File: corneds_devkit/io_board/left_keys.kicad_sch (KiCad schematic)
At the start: 42 parts, among them SW1 SW_Push, SW10 SW_Push, SW11 SW_Push, SW12 SW_Push, SW13 SW_Push, SW15 SW_Push, SW17 SW_Push, SW19 SW_Push, SW2 SW_Push, SW20 SW_Push, SW21 SW_Push, SW22 SW_Push, SW23 SW_Push, SW24 SW_Push, SW3 SW_Push, SW4 SW_Push, SW5 SW_Push, SW6 SW_Push, SW7 SW_Push, SW8 SW_Push, SW9 SW_Push

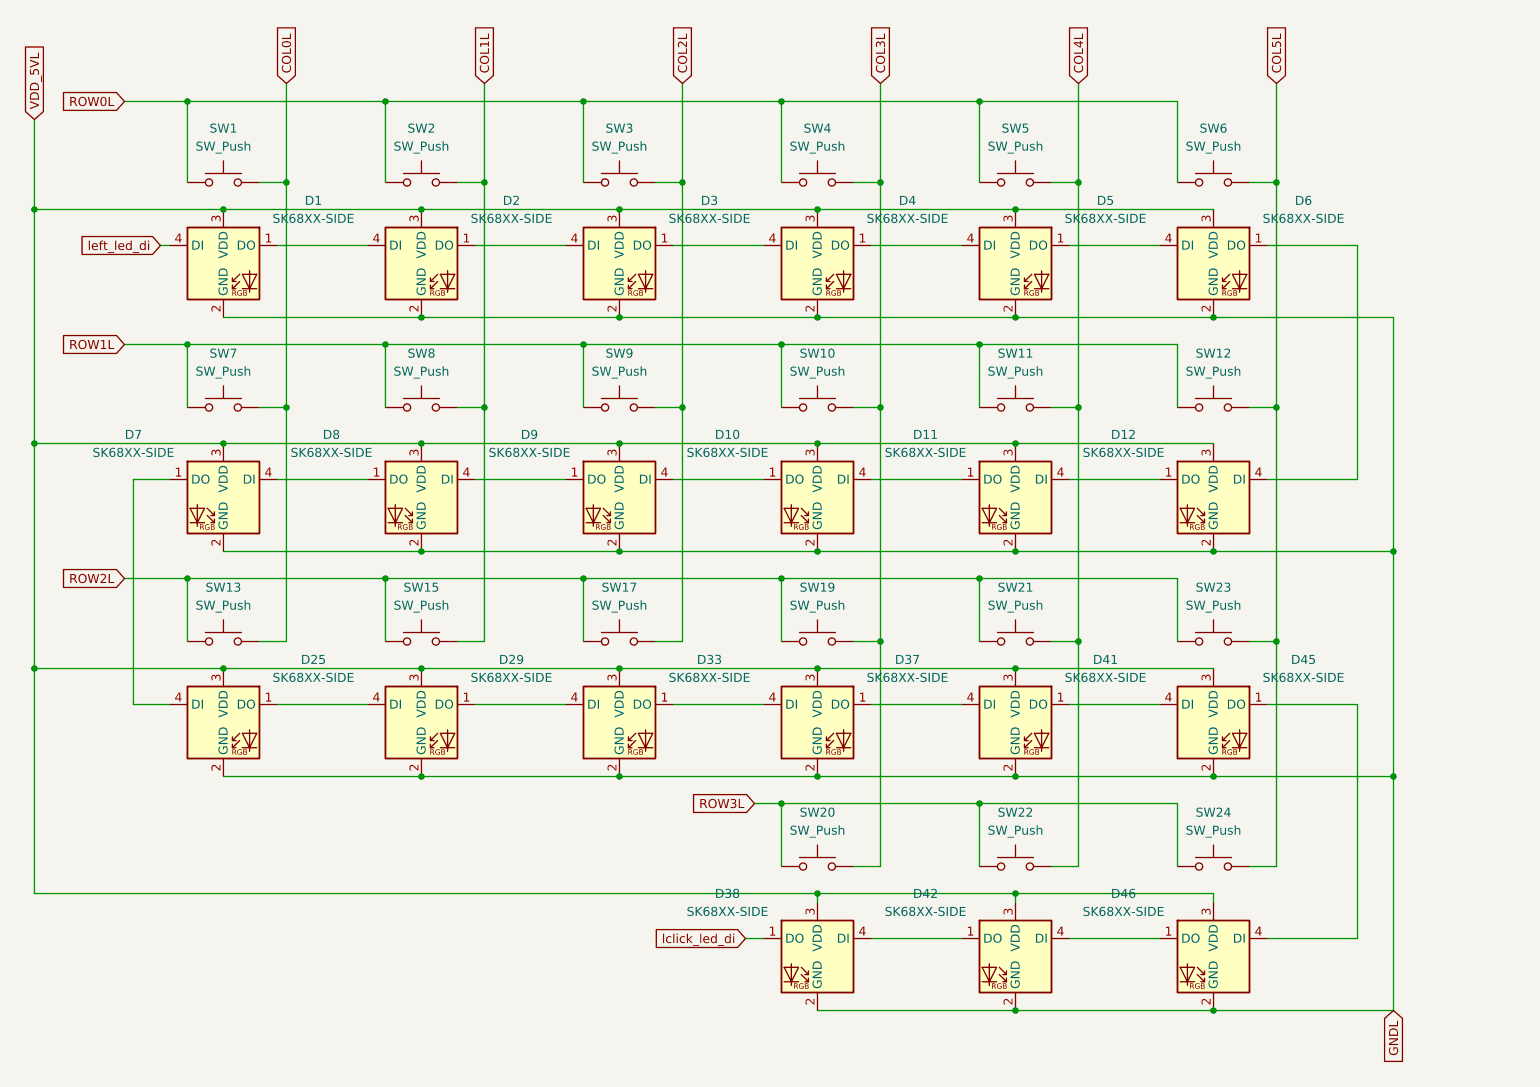
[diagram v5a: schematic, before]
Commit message: routing left keys pcb
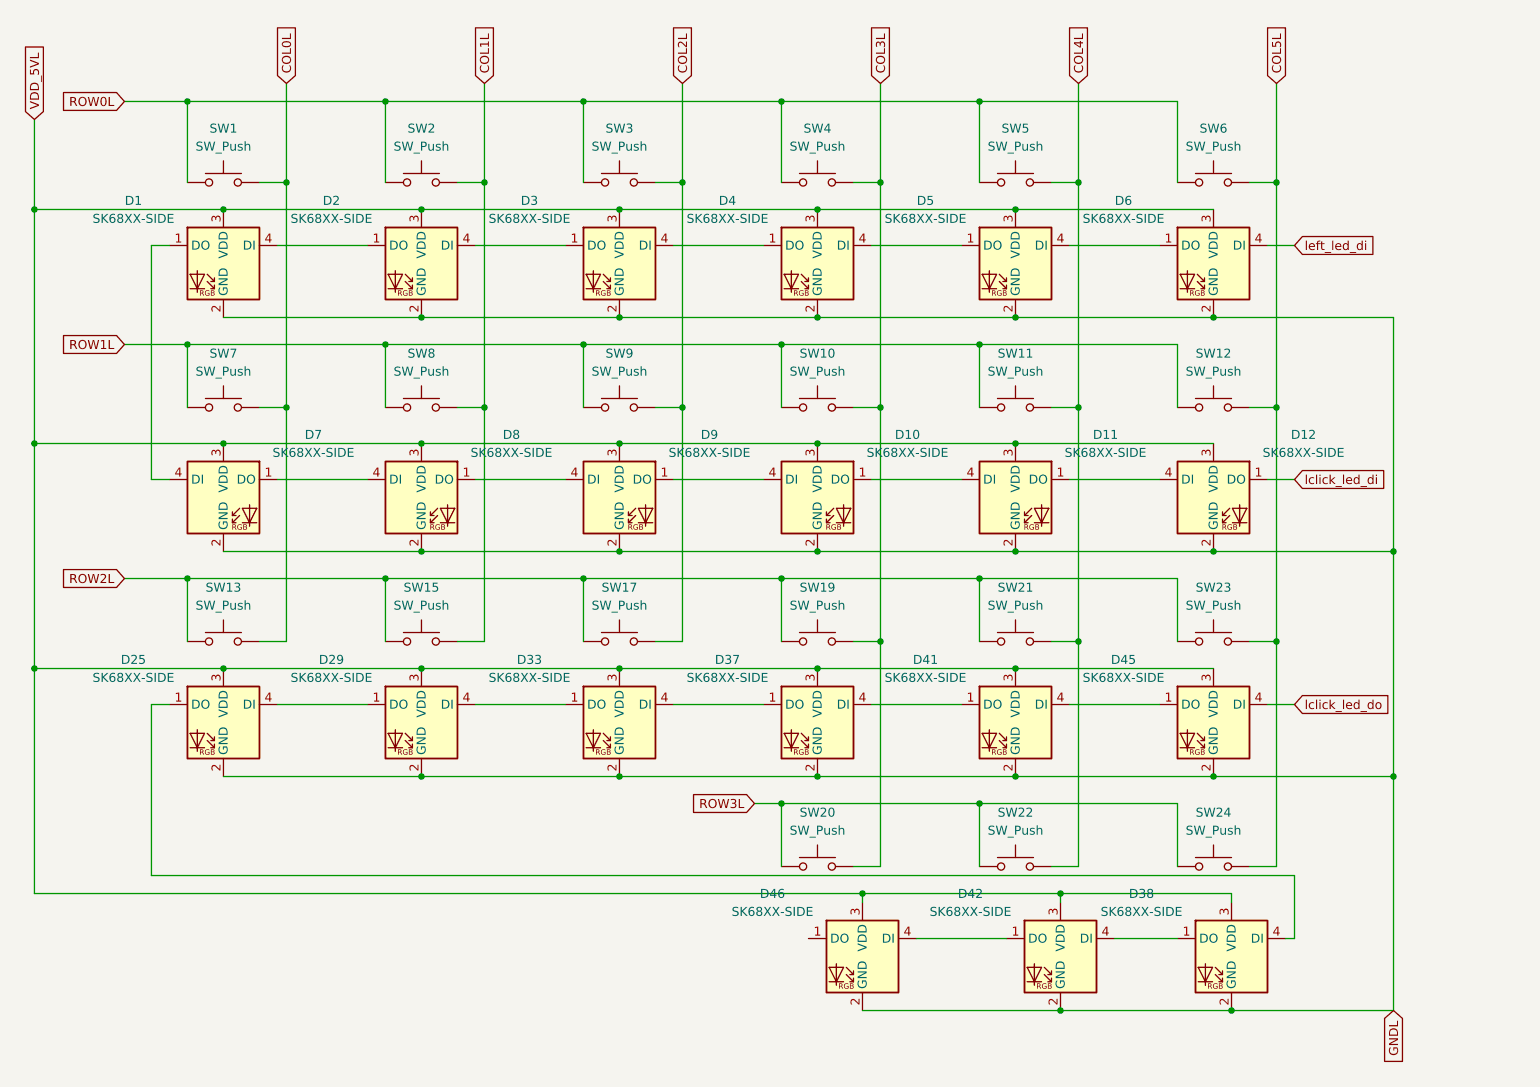
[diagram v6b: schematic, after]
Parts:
- SW1, SW10, SW11, SW12, SW13, SW15, SW17, SW19, SW2, SW20, SW21, SW22, SW23, SW24, SW3, SW4, SW5, SW6, SW7, SW8, SW9: footprint key-switches:SW_Gateron_LowProfile_HotSwap_THT -> key-switches:SW_Gateron_LowProfile_HotSwap_PTH
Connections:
- net lclick_led_di: now also D12.1 (DO); no longer D38.1 (DO)
- net left_led_di: now also D6.4 (DI); no longer D1.4 (DI)
- net at D25.1 (DO): now also D38.4 (DI); no longer D29.4 (DI)
- net at D25.4 (DI): now also D29.1 (DO); no longer D7.1 (DO)
- net at D1.1 (DO): now also D7.4 (DI); no longer D2.4 (DI)
- net at D4.1 (DO): now also D3.4 (DI); no longer D5.4 (DI)
- net at D4.4 (DI): now also D5.1 (DO); no longer D3.1 (DO)
- net at D41.1 (DO): now also D37.4 (DI); no longer D45.4 (DI)
- net at D41.4 (DI): now also D45.1 (DO); no longer D37.1 (DO)
- net at D42.1 (DO): now also D46.4 (DI); no longer D38.4 (DI)
- net at D42.4 (DI): now also D38.1 (DO); no longer D46.1 (DO)
- net at D33.4 (DI): now also D37.1 (DO); no longer D29.1 (DO)
- net at D6.1 (DO): now also D5.4 (DI); no longer D12.4 (DI)
- net at D33.1 (DO): now also D29.4 (DI); no longer D37.4 (DI)
- net at D11.1 (DO): now also D12.4 (DI); no longer D10.4 (DI)
- net at D11.4 (DI): now also D10.1 (DO); no longer D12.1 (DO)
- net at D8.1 (DO): now also D9.4 (DI); no longer D7.4 (DI)
- net at D8.4 (DI): now also D7.1 (DO); no longer D9.1 (DO)
- net at D2.1 (DO): now also D1.4 (DI); no longer D3.4 (DI)
- new net: D10.4 (DI), D9.1 (DO)
- new net: D2.4 (DI), D3.1 (DO)
- new net lclick_led_do: D45.4 (DI)
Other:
- moved on the sheet: D38, D42, D46

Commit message: finished routing power board and started on control board schematic but realized I need seperate reset lines
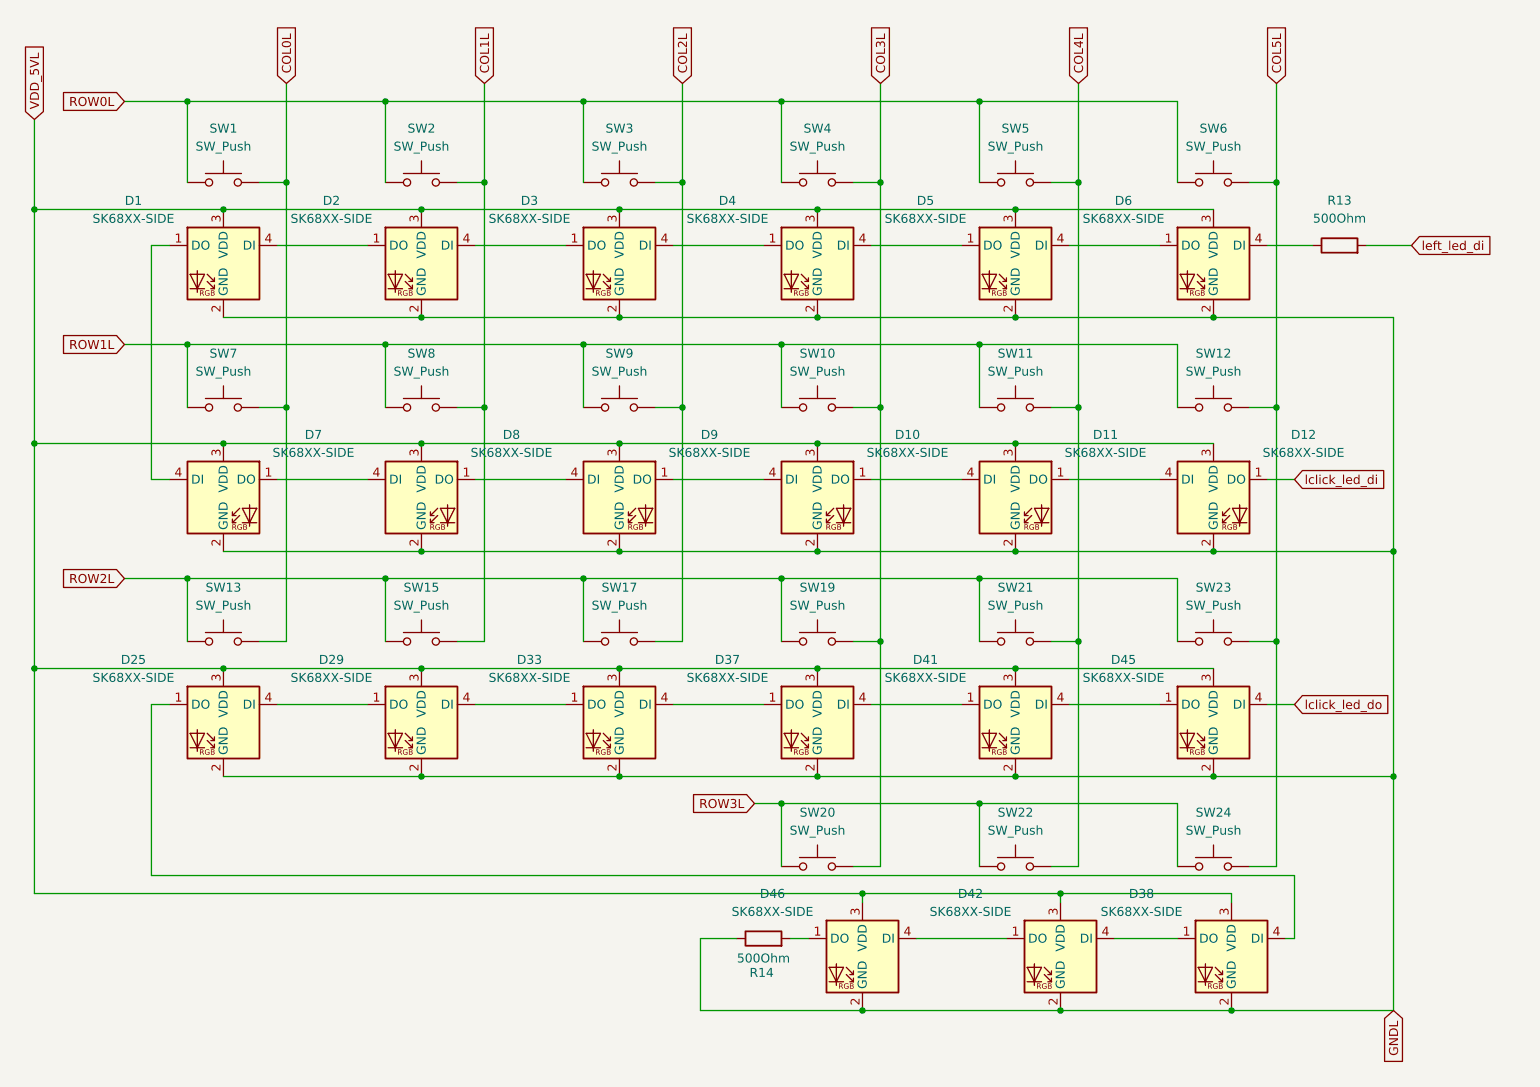
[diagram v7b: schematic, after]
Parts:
- added R13, R14: 500Ohm, Resistor_SMD:R_0402_1005Metric, symbol Device:R
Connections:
- net GNDL: now also R14.1
- net left_led_di: now also R13.2; no longer D6.4 (DI)
- net at D46.1 (DO): now also R14.2
- new net: D6.4 (DI), R13.1
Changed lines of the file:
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@@
 	)
 	(junction
+		(at 180.34 152.4)
+		(diameter 0)
+		(color 0 0 0 0)
+	)
+	(junction
 		(at 63.5 104.14)
 		(diameter 0)
@@
 	(wire
 		(pts
+			(xy 170.18 142.24) (xy 172.72 142.24)
+		)
+		(stroke
+			(width 0)
+			(type default)
+		)
+	)
+	(wire
+		(pts
 			(xy 182.88 100.33) (xy 182.88 67.31)
 		)
@@
 	(wire
 		(pts
-			(xy 237.49 44.45) (xy 241.3 44.45)
+			(xy 123.19 100.33) (xy 127 100.33)
 		)
 		(stroke
@@
 	(wire
 		(pts
-			(xy 123.19 100.33) (xy 127 100.33)
+			(xy 229.87 87.63) (xy 255.27 87.63)
 		)
 		(stroke
@@
 	(wire
 		(pts
-			(xy 229.87 87.63) (xy 255.27 87.63)
+			(xy 157.48 152.4) (xy 180.34 152.4)
 		)
 		(stroke
@@
 	(wire
 		(pts
+			(xy 162.56 142.24) (xy 157.48 142.24)
+		)
+		(stroke
+			(width 0)
+			(type default)
+		)
+	)
+	(wire
+		(pts
 			(xy 173.99 39.37) (xy 201.93 39.37)
 		)
@@
 	(wire
 		(pts
+			(xy 251.46 44.45) (xy 257.81 44.45)
+		)
+		(stroke
+			(width 0)
+			(type default)
+		)
+	)
+	(wire
+		(pts
 			(xy 85.09 24.13) (xy 76.2 24.13)
 		)
@@
 	(wire
 		(pts
+			(xy 157.48 142.24) (xy 157.48 152.4)
+		)
+		(stroke
+			(width 0)
+			(type default)
+		)
+	)
+	(wire
+		(pts
 			(xy 168.91 91.44) (xy 140.97 91.44)
 		)
@@
 	(wire
 		(pts
+			(xy 237.49 44.45) (xy 243.84 44.45)
+		)
+		(stroke
+			(width 0)
+			(type default)
+		)
+	)
+	(wire
+		(pts
 			(xy 201.93 104.14) (xy 229.87 104.14)
 		)
@@
 	(global_label "left_led_di"
 		(shape input)
-		(at 241.3 44.45 0)
+		(at 257.81 44.45 0)
 		(fields_autoplaced yes)
 		(effects
@@
 		)
 		(property "Intersheetrefs" "${INTERSHEET_REFS}"
-			(at 254.0822 44.45 0)
+			(at 270.5922 44.45 0)
 			(effects
 				(font
@@
 	)
 	(symbol
+		(lib_id "Device:R")
+		(at 166.37 142.24 90)
+		(unit 1)
+		(exclude_from_sim no)
+		(in_bom yes)
+		(on_board yes)
+		(dnp no)
+		(property "Reference" "R14"
+			(at 166.116 147.066 90)
+			(effects
+				(font
+					(size 1.27 1.27)
+				)
+			)
+		)
+		(property "Value" "500Ohm"
+			(at 166.37 145.034 90)
+			(effects
+				(font
+					(size 1.27 1.27)
+				)
+			)
+		)
+		(property "Footprint" "Resistor_SMD:R_0402_1005Metric"
+			(at 166.37 144.018 90)
+			(effects
+				(font
+					(size 1.27 1.27)
+				)
+				(hide yes)
+			)
+		)
+		(property "Datasheet" "~"
+			(at 166.37 142.24 0)
+			(effects
+				(font
+					(size 1.27 1.27)
+				)
+				(hide yes)
+			)
+		)
+		(property "Description" "Resistor"
+			(at 166.37 142.24 0)
+			(effects
+				(font
+					(size 1.27 1.27)
+				)
+				(hide yes)
+			)
+		)
+		(pin "1"
+		)
+		(pin "2"
+		)
+		(instances
+			(project "io_board"
+				(path "/244b6d6b-132d-4d50-ae86-e41103b29008/035ff8de-23b0-4e40-a4d6-13420d9ceca3"
+					(reference "R14")
+					(unit 1)
+				)
+			)
+		)
+	)
+	(symbol
 		(lib_id "Switch:SW_Push")
 		(at 229.87 100.33 0)
@@
 					(unit 1)
 				)
+			)
+		)
+	)
+	(symbol
+		(lib_id "Device:R")
+		(at 247.65 44.45 90)
+		(unit 1)
+		(exclude_from_sim no)
+		(in_bom yes)
+		(on_board yes)
+		(dnp no)
+		(fields_autoplaced yes)
+		(property "Reference" "R13"
+			(at 247.65 38.1 90)
+			(effects
+				(font
+					(size 1.27 1.27)
+				)
+			)
+		)
+		(property "Value" "500Ohm"
+			(at 247.65 40.64 90)
+			(effects
+				(font
+					(size 1.27 1.27)
+				)
+			)
+		)
+		(property "Footprint" "Resistor_SMD:R_0402_1005Metric"
+			(at 247.65 46.228 90)
+			(effects
+				(font
+					(size 1.27 1.27)
+				)
+				(hide yes)
+			)
+		)
+		(property "Datasheet" "~"
+			(at 247.65 44.45 0)
+			(effects
+				(font
+					(size 1.27 1.27)
+				)
+				(hide yes)
+			)
+		)
+		(property "Description" "Resistor"
+			(at 247.65 44.45 0)
+			(effects
+				(font
+					(size 1.27 1.27)
+				)
+				(hide yes)
+			)
+		)
+		(pin "1"
+		)
+		(pin "2"
+		)
+		(instances
+			(project "io_board"
+				(path "/244b6d6b-132d-4d50-ae86-e41103b29008/035ff8de-23b0-4e40-a4d6-13420d9ceca3"
+					(reference "R13")
+					(unit 1)
+				)
